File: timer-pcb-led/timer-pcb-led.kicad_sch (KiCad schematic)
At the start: 10 parts, among them J1 JST_03

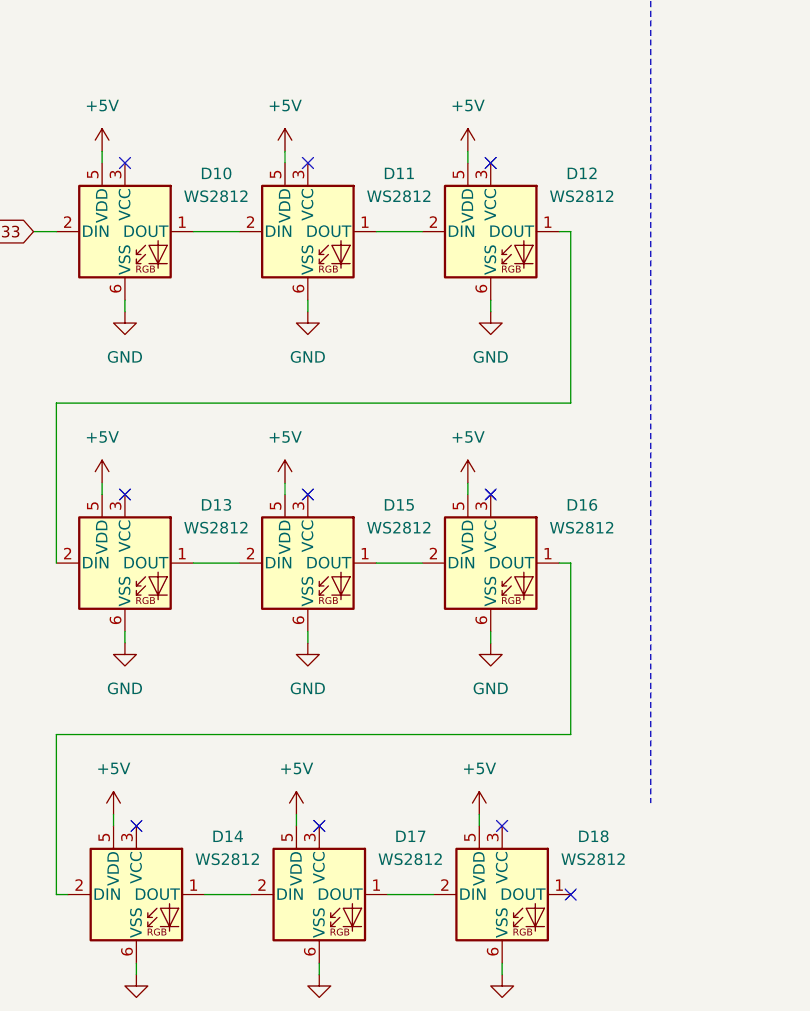
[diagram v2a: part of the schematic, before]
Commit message: suppression du dossier chargeur. integration de la partie chargeur usb-c sur le PCB stepper
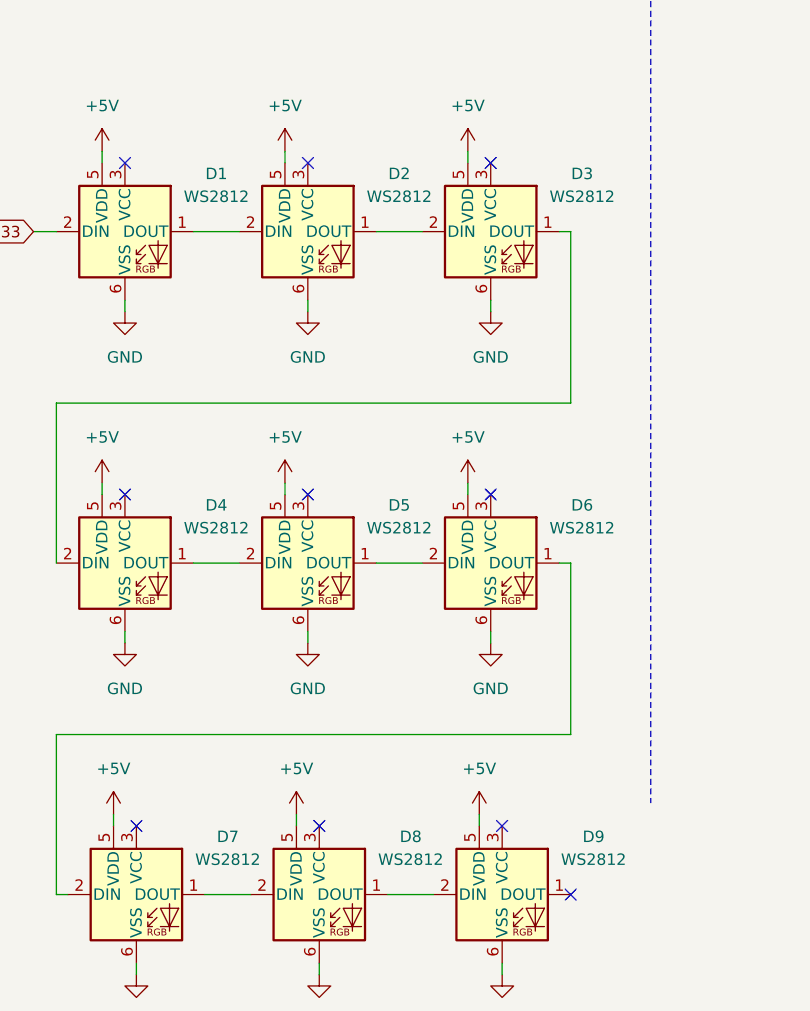
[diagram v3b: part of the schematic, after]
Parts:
- renumbered D10 to D1, D11 to D2, D12 to D3, D13 to D4, D15 to D5, D16 to D6, D14 to D7, D17 to D8, D18 to D9
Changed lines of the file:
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@@
 		(on_board yes)
 		(dnp no)
-		(property "Reference" "D14"
+		(property "Reference" "D7"
 			(at 130.81 170.1098 0)
 			(effects
@@
 			(project "Timer_PCB"
 				(path "/c4cfdf40-c3b2-4c58-998c-a7d7b70b9691"
-					(reference "D14")
+					(reference "D7")
 					(unit 1)
 				)
@@
 		(on_board yes)
 		(dnp no)
-		(property "Reference" "D15"
+		(property "Reference" "D5"
 			(at 149.86 133.2798 0)
 			(effects
@@
 			(project "Timer_PCB"
 				(path "/c4cfdf40-c3b2-4c58-998c-a7d7b70b9691"
-					(reference "D15")
+					(reference "D5")
 					(unit 1)
 				)
@@
 		(on_board yes)
 		(dnp no)
-		(property "Reference" "D18"
+		(property "Reference" "D9"
 			(at 171.45 170.1098 0)
 			(effects
@@
 			(project "Timer_PCB"
 				(path "/c4cfdf40-c3b2-4c58-998c-a7d7b70b9691"
-					(reference "D18")
+					(reference "D9")
 					(unit 1)
 				)
@@
 		(dnp no)
 		(fields_autoplaced yes)
-		(property "Reference" "#PWR023"
+		(property "Reference" "#PWR014"
 			(at 119.38 154.94 0)
 			(effects
@@
 			(project "Timer_PCB"
 				(path "/c4cfdf40-c3b2-4c58-998c-a7d7b70b9691"
-					(reference "#PWR023")
+					(reference "#PWR014")
 					(unit 1)
 				)
@@
 		(dnp no)
 		(fields_autoplaced yes)
-		(property "Reference" "#PWR022"
+		(property "Reference" "#PWR011"
 			(at 116.84 134.62 0)
 			(effects
@@
 			(project "Timer_PCB"
 				(path "/c4cfdf40-c3b2-4c58-998c-a7d7b70b9691"
-					(reference "#PWR022")
+					(reference "#PWR011")
 					(unit 1)
 				)
@@
 		(dnp no)
 		(fields_autoplaced yes)
-		(property "Reference" "#PWR030"
+		(property "Reference" "#PWR018"
 			(at 138.43 171.45 0)
 			(effects
@@
 			(project "Timer_PCB"
 				(path "/c4cfdf40-c3b2-4c58-998c-a7d7b70b9691"
-					(reference "#PWR030")
+					(reference "#PWR018")
 					(unit 1)
 				)
@@
 		(dnp no)
 		(fields_autoplaced yes)
-		(property "Reference" "#PWR032"
+		(property "Reference" "#PWR019"
 			(at 158.75 171.45 0)
 			(effects
@@
 			(project "Timer_PCB"
 				(path "/c4cfdf40-c3b2-4c58-998c-a7d7b70b9691"
-					(reference "#PWR032")
+					(reference "#PWR019")
 					(unit 1)
 				)
@@
 		(dnp no)
 		(fields_autoplaced yes)
-		(property "Reference" "#PWR012"
+		(property "Reference" "#PWR03"
 			(at 116.84 97.79 0)
 			(effects
@@
 			(project "Timer_PCB"
 				(path "/c4cfdf40-c3b2-4c58-998c-a7d7b70b9691"
-					(reference "#PWR012")
+					(reference "#PWR03")
 					(unit 1)
 				)
@@
 		(dnp no)
 		(fields_autoplaced yes)
-		(property "Reference" "#PWR016"
+		(property "Reference" "#PWR01"
 			(at 35.56 96.52 0)
 			(effects
@@
 			(project "timer-pcb-led"
 				(path "/c4cfdf40-c3b2-4c58-998c-a7d7b70b9691"
-					(reference "#PWR016")
+					(reference "#PWR01")
 					(unit 1)
 				)
@@
 		(dnp no)
 		(fields_autoplaced yes)
-		(property "Reference" "#PWR020"
+		(property "Reference" "#PWR05"
 			(at 157.48 97.79 0)
 			(effects
@@
 			(project "Timer_PCB"
 				(path "/c4cfdf40-c3b2-4c58-998c-a7d7b70b9691"
-					(reference "#PWR020")
+					(reference "#PWR05")
 					(unit 1)
 				)
@@
 		(dnp no)
 		(fields_autoplaced yes)
-		(property "Reference" "#PWR025"
+		(property "Reference" "#PWR020"
 			(at 120.65 191.77 0)
 			(effects
@@
 			(project "Timer_PCB"
 				(path "/c4cfdf40-c3b2-4c58-998c-a7d7b70b9691"
-					(reference "#PWR025")
+					(reference "#PWR020")
 					(unit 1)
 				)
@@
 		(on_board yes)
 		(dnp no)
-		(property "Reference" "D12"
+		(property "Reference" "D3"
 			(at 170.18 96.4498 0)
 			(effects
@@
 			(project "Timer_PCB"
 				(path "/c4cfdf40-c3b2-4c58-998c-a7d7b70b9691"
-					(reference "D12")
+					(reference "D3")
 					(unit 1)
 				)
@@
 		(dnp no)
 		(fields_autoplaced yes)
-		(property "Reference" "#PWR029"
+		(property "Reference" "#PWR016"
 			(at 160.02 154.94 0)
 			(effects
@@
 			(project "Timer_PCB"
 				(path "/c4cfdf40-c3b2-4c58-998c-a7d7b70b9691"
-					(reference "#PWR029")
+					(reference "#PWR016")
 					(unit 1)
 				)
@@
 		(dnp no)
 		(fields_autoplaced yes)
-		(property "Reference" "#PWR026"
+		(property "Reference" "#PWR012"
 			(at 137.16 134.62 0)
 			(effects
@@
 			(project "Timer_PCB"
 				(path "/c4cfdf40-c3b2-4c58-998c-a7d7b70b9691"
-					(reference "#PWR026")
+					(reference "#PWR012")
 					(unit 1)
 				)
@@
 		(dnp no)
 		(fields_autoplaced yes)
-		(property "Reference" "#PWR024"
+		(property "Reference" "#PWR017"
 			(at 118.11 171.45 0)
 			(effects
@@
 			(project "Timer_PCB"
 				(path "/c4cfdf40-c3b2-4c58-998c-a7d7b70b9691"
-					(reference "#PWR024")
+					(reference "#PWR017")
 					(unit 1)
 				)
@@
 		(on_board yes)
 		(dnp no)
-		(property "Reference" "#PWR017"
+		(property "Reference" "#PWR06"
 			(at 35.56 110.49 0)
 			(effects
@@
 			(project "timer-pcb-led"
 				(path "/c4cfdf40-c3b2-4c58-998c-a7d7b70b9691"
-					(reference "#PWR017")
+					(reference "#PWR06")
 					(unit 1)
 				)
@@
 		(dnp no)
 		(fields_autoplaced yes)
-		(property "Reference" "#PWR028"
+		(property "Reference" "#PWR013"
 			(at 157.48 134.62 0)
 			(effects
@@
 			(project "Timer_PCB"
 				(path "/c4cfdf40-c3b2-4c58-998c-a7d7b70b9691"
-					(reference "#PWR028")
+					(reference "#PWR013")
 					(unit 1)
 				)
@@
 		(on_board yes)
 		(dnp no)
-		(property "Reference" "D16"
+		(property "Reference" "D6"
 			(at 170.18 133.2798 0)
 			(effects
@@
 			(project "Timer_PCB"
 				(path "/c4cfdf40-c3b2-4c58-998c-a7d7b70b9691"
-					(reference "D16")
+					(reference "D6")
 					(unit 1)
 				)
@@
 		(dnp no)
 		(fields_autoplaced yes)
-		(property "Reference" "#PWR013"
+		(property "Reference" "#PWR07"
 			(at 119.38 118.11 0)
 			(effects
@@
 			(project "Timer_PCB"
 				(path "/c4cfdf40-c3b2-4c58-998c-a7d7b70b9691"
-					(reference "#PWR013")
+					(reference "#PWR07")
 					(unit 1)
 				)
@@
 		(dnp no)
 		(fields_autoplaced yes)
-		(property "Reference" "#PWR019"
+		(property "Reference" "#PWR08"
 			(at 139.7 118.11 0)
 			(effects
@@
 			(project "Timer_PCB"
 				(path "/c4cfdf40-c3b2-4c58-998c-a7d7b70b9691"
-					(reference "#PWR019")
+					(reference "#PWR08")
 					(unit 1)
 				)
@@
 		(dnp no)
 		(fields_autoplaced yes)
-		(property "Reference" "#PWR027"
+		(property "Reference" "#PWR015"
 			(at 139.7 154.94 0)
 			(effects
@@
 			(project "Timer_PCB"
 				(path "/c4cfdf40-c3b2-4c58-998c-a7d7b70b9691"
-					(reference "#PWR027")
+					(reference "#PWR015")
 					(unit 1)
 				)
@@
 		(dnp no)
 		(fields_autoplaced yes)
-		(property "Reference" "#PWR021"
+		(property "Reference" "#PWR09"
 			(at 160.02 118.11 0)
 			(effects
@@
 			(project "Timer_PCB"
 				(path "/c4cfdf40-c3b2-4c58-998c-a7d7b70b9691"
-					(reference "#PWR021")
+					(reference "#PWR09")
 					(unit 1)
 				)
@@
 		(dnp no)
 		(fields_autoplaced yes)
-		(property "Reference" "#PWR018"
+		(property "Reference" "#PWR04"
 			(at 137.16 97.79 0)
 			(effects
@@
 			(project "Timer_PCB"
 				(path "/c4cfdf40-c3b2-4c58-998c-a7d7b70b9691"
-					(reference "#PWR018")
+					(reference "#PWR04")
 					(unit 1)
 				)
@@
 		(dnp no)
 		(fields_autoplaced yes)
-		(property "Reference" "#PWR031"
+		(property "Reference" "#PWR021"
 			(at 140.97 191.77 0)
 			(effects
@@
 			(project "Timer_PCB"
 				(path "/c4cfdf40-c3b2-4c58-998c-a7d7b70b9691"
-					(reference "#PWR031")
+					(reference "#PWR021")
 					(unit 1)
 				)
@@
 		(on_board yes)
 		(dnp no)
-		(property "Reference" "D11"
+		(property "Reference" "D2"
 			(at 149.86 96.4498 0)
 			(effects
@@
 			(project "Timer_PCB"
 				(path "/c4cfdf40-c3b2-4c58-998c-a7d7b70b9691"
-					(reference "D11")
+					(reference "D2")
 					(unit 1)
 				)
@@
 		(dnp no)
 		(fields_autoplaced yes)
-		(property "Reference" "#PWR015"
+		(property "Reference" "#PWR010"
 			(at 80.01 119.38 0)
 			(effects
@@
 			(project "timer-pcb-led"
 				(path "/c4cfdf40-c3b2-4c58-998c-a7d7b70b9691"
-					(reference "#PWR015")
+					(reference "#PWR010")
 					(unit 1)
 				)
@@
 		(on_board yes)
 		(dnp no)
-		(property "Reference" "D17"
+		(property "Reference" "D8"
 			(at 151.13 170.1098 0)
 			(effects
@@
 			(project "Timer_PCB"
 				(path "/c4cfdf40-c3b2-4c58-998c-a7d7b70b9691"
-					(reference "D17")
+					(reference "D8")
 					(unit 1)
 				)
@@
 		(on_board yes)
 		(dnp no)
-		(property "Reference" "D10"
+		(property "Reference" "D1"
 			(at 129.54 96.4498 0)
 			(effects
@@
 			(project "Timer_PCB"
 				(path "/c4cfdf40-c3b2-4c58-998c-a7d7b70b9691"
-					(reference "D10")
+					(reference "D1")
 					(unit 1)
 				)
@@
 		(dnp no)
 		(fields_autoplaced yes)
-		(property "Reference" "#PWR014"
+		(property "Reference" "#PWR02"
 			(at 80.01 97.79 0)
 			(effects
@@
 			(project "timer-pcb-led"
 				(path "/c4cfdf40-c3b2-4c58-998c-a7d7b70b9691"
-					(reference "#PWR014")
+					(reference "#PWR02")
 					(unit 1)
 				)
@@
 		(on_board yes)
 		(dnp no)
-		(property "Reference" "D13"
+		(property "Reference" "D4"
 			(at 129.54 133.2798 0)
 			(effects
@@
 			(project "Timer_PCB"
 				(path "/c4cfdf40-c3b2-4c58-998c-a7d7b70b9691"
-					(reference "D13")
+					(reference "D4")
 					(unit 1)
 				)
@@
 		(dnp no)
 		(fields_autoplaced yes)
-		(property "Reference" "#PWR033"
+		(property "Reference" "#PWR022"
 			(at 161.29 191.77 0)
 			(effects
@@
 			(project "Timer_PCB"
 				(path "/c4cfdf40-c3b2-4c58-998c-a7d7b70b9691"
-					(reference "#PWR033")
-					(unit 1)
-				)
+					(reference "#PWR022")
+					(unit 1)
+				)

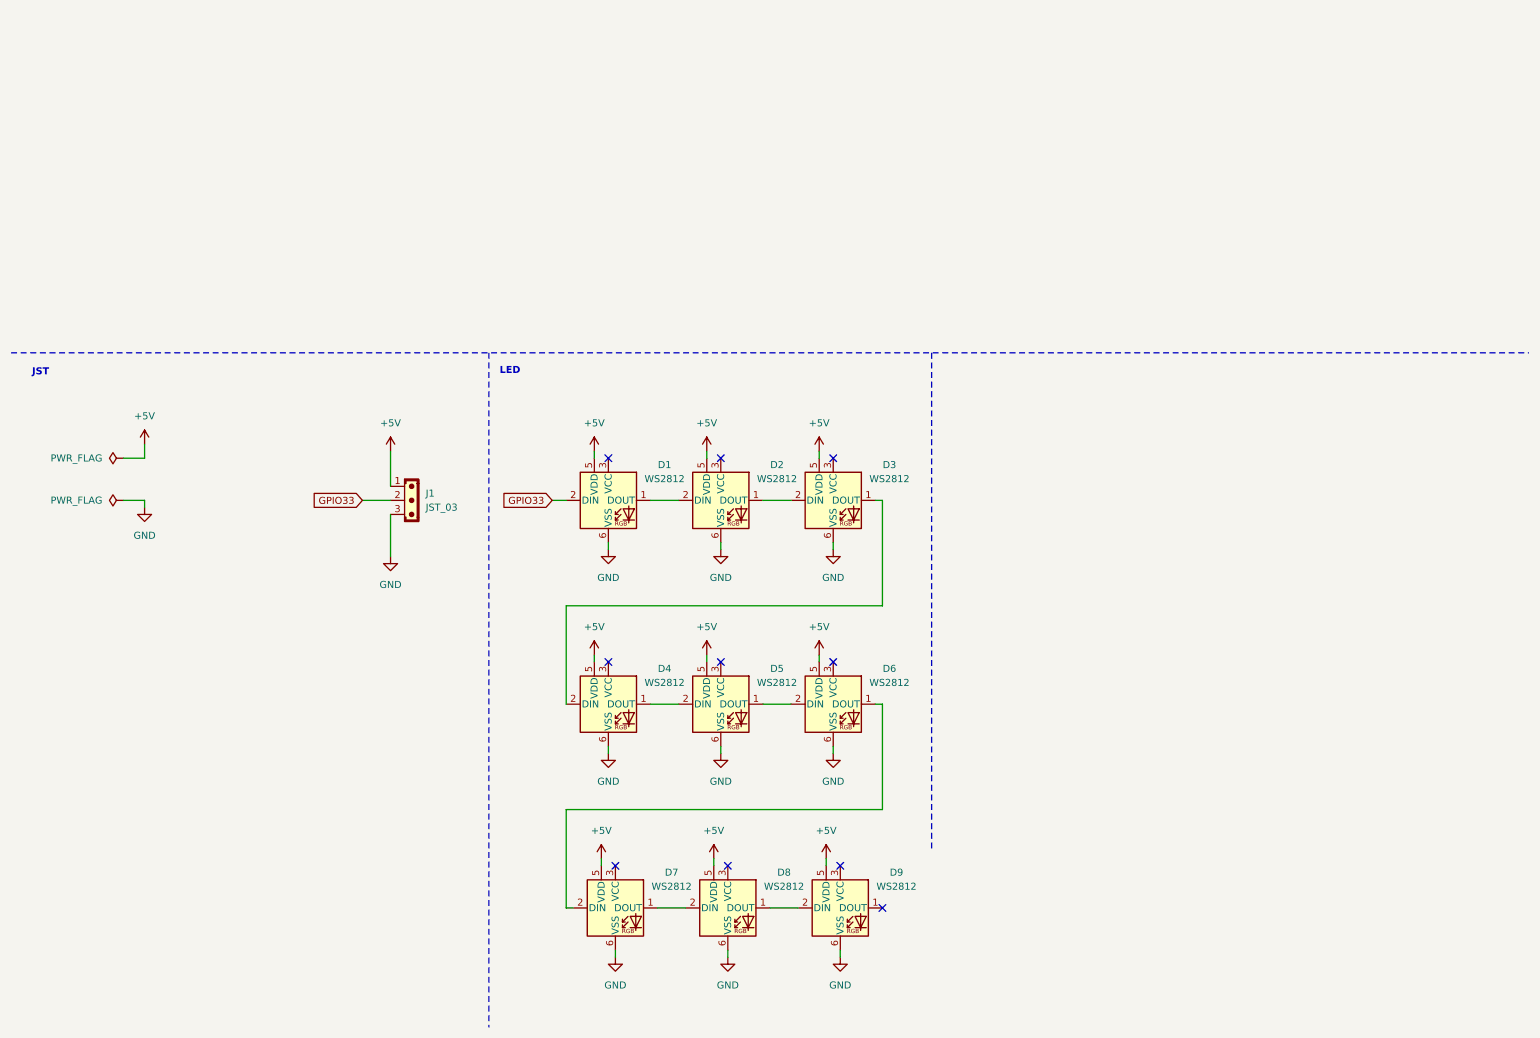
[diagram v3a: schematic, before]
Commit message: mise à jour fichier blender pour impression 3D. Reste a mettre la bonne épaisseur pour le socle de la shell et percer les trous pour interrupteurs switch et on-off. déterminer ou placer entrées pour recharge et update code. comment fixer module recharge.
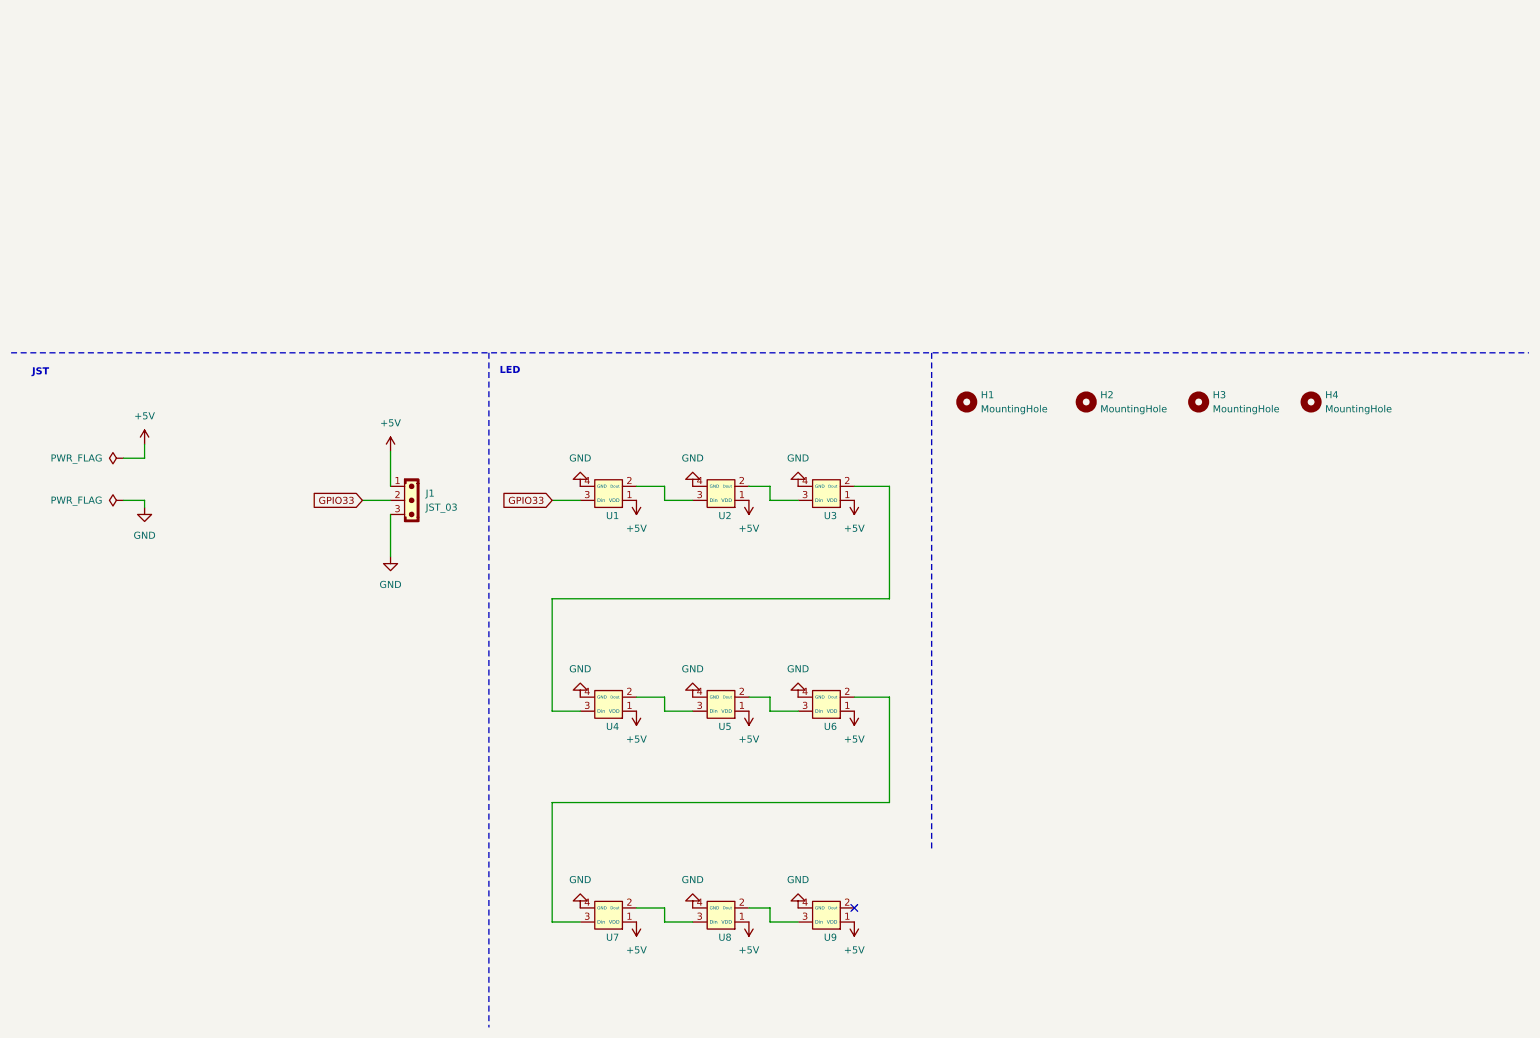
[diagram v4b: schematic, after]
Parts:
- removed D1, D2, D3, D4, D5, D6, D7, D8, D9: WS2812, LED_SMD:LED_WS2812_PLCC6_5.0x5.0mm_P1.6mm, symbol LED:WS2812
- added H1, H2, H3, H4: MountingHole, MountingHole:MountingHole_3.2mm_M3_DIN965_Pad_TopOnly, symbol Mechanical:MountingHole
- added U1, U2, U3, U4, U5, U6, U7, U8, U9: ~, 1_My_Custom_Library:WS2812B-Xinlight-5050RGBC, symbol 1_my_custom-_symbol_library:WS2812B-XingLight-5050RGBC-
- J1: now left out of the parts list
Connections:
- net +5V: now also U1.1 (VDD), U2.1 (VDD), U3.1 (VDD), U4.1 (VDD), U5.1 (VDD), U6.1 (VDD), U7.1 (VDD), U8.1 (VDD), U9.1 (VDD)
- net GND: now also U1.4 (GND), U2.4 (GND), U3.4 (GND), U4.4 (GND), U5.4 (GND), U6.4 (GND), U7.4 (GND), U8.4 (GND), U9.4 (GND)
- net GPIO33: now also U1.3 (Din)
- new net: U8.2 (Dout), U9.3 (Din)
- new net: U7.2 (Dout), U8.3 (Din)
- new net: U3.2 (Dout), U4.3 (Din)
- new net: U2.2 (Dout), U3.3 (Din)
- new net: U6.2 (Dout), U7.3 (Din)
- new net: U5.2 (Dout), U6.3 (Din)
- new net: U1.2 (Dout), U2.3 (Din)
- new net: U4.2 (Dout), U5.3 (Din)
- no-connect marks 10 -> 1
